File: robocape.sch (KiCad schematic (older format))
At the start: 22 parts

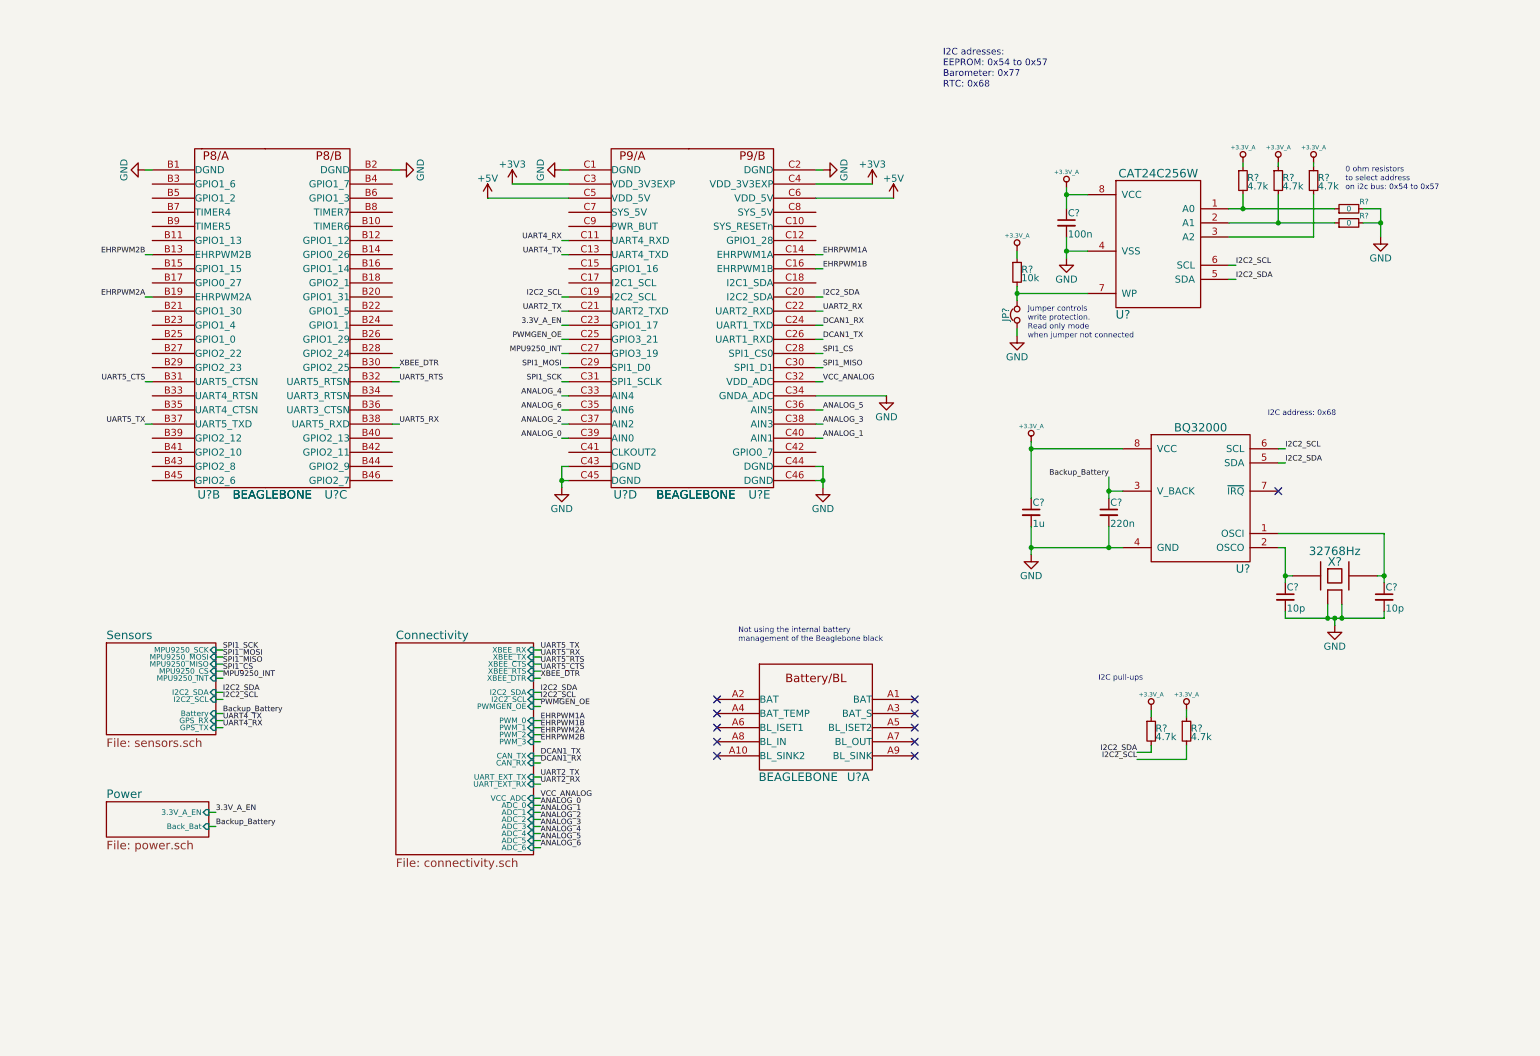
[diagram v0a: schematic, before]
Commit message: Schematics: Minor cleanups
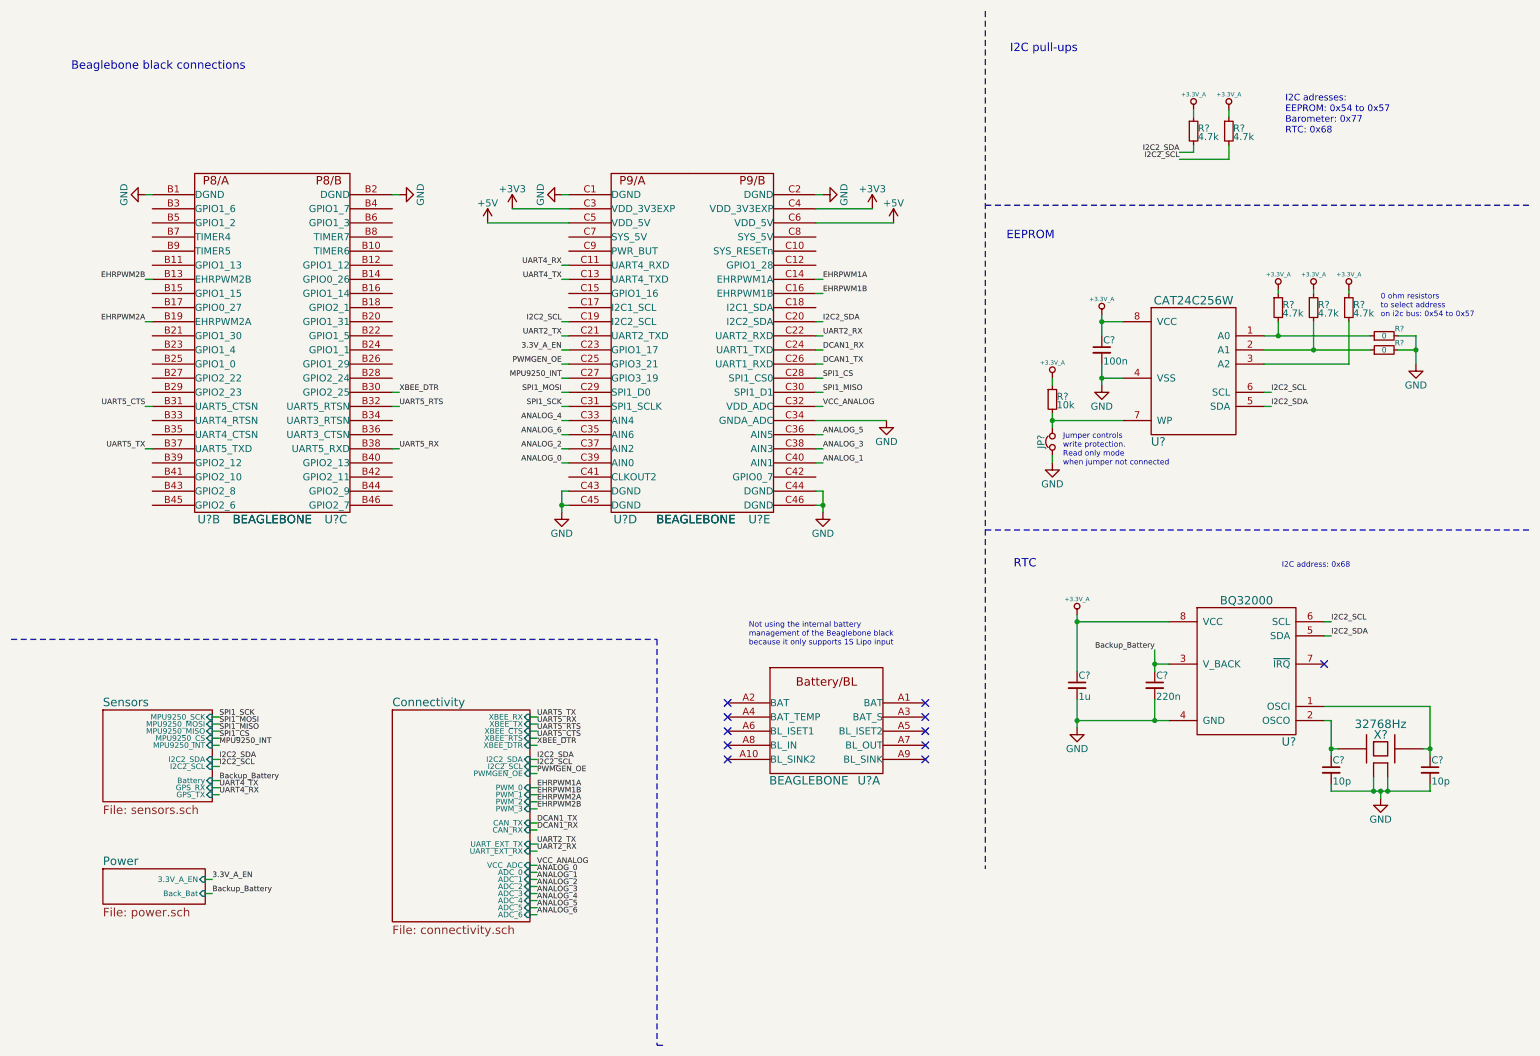
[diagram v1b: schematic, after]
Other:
- note added: "Beaglebone black connections"
- note added: "EEPROM\n"
- note added: "I2C pull-ups"
- note added: "Not using the internal battery\nmanagement of the Beaglebone black\nbecause it only supports 1S Lipo input"
- note added: "RTC"
- note removed: "I2C pull-ups\n"
- note removed: "Not using the internal battery\nmanagement of the Beaglebone black"
- moved on the sheet: C?, JP?, R?, U?, U?A, U?B, U?C, U?D, U?E, X?

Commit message: Schematics: LEDs
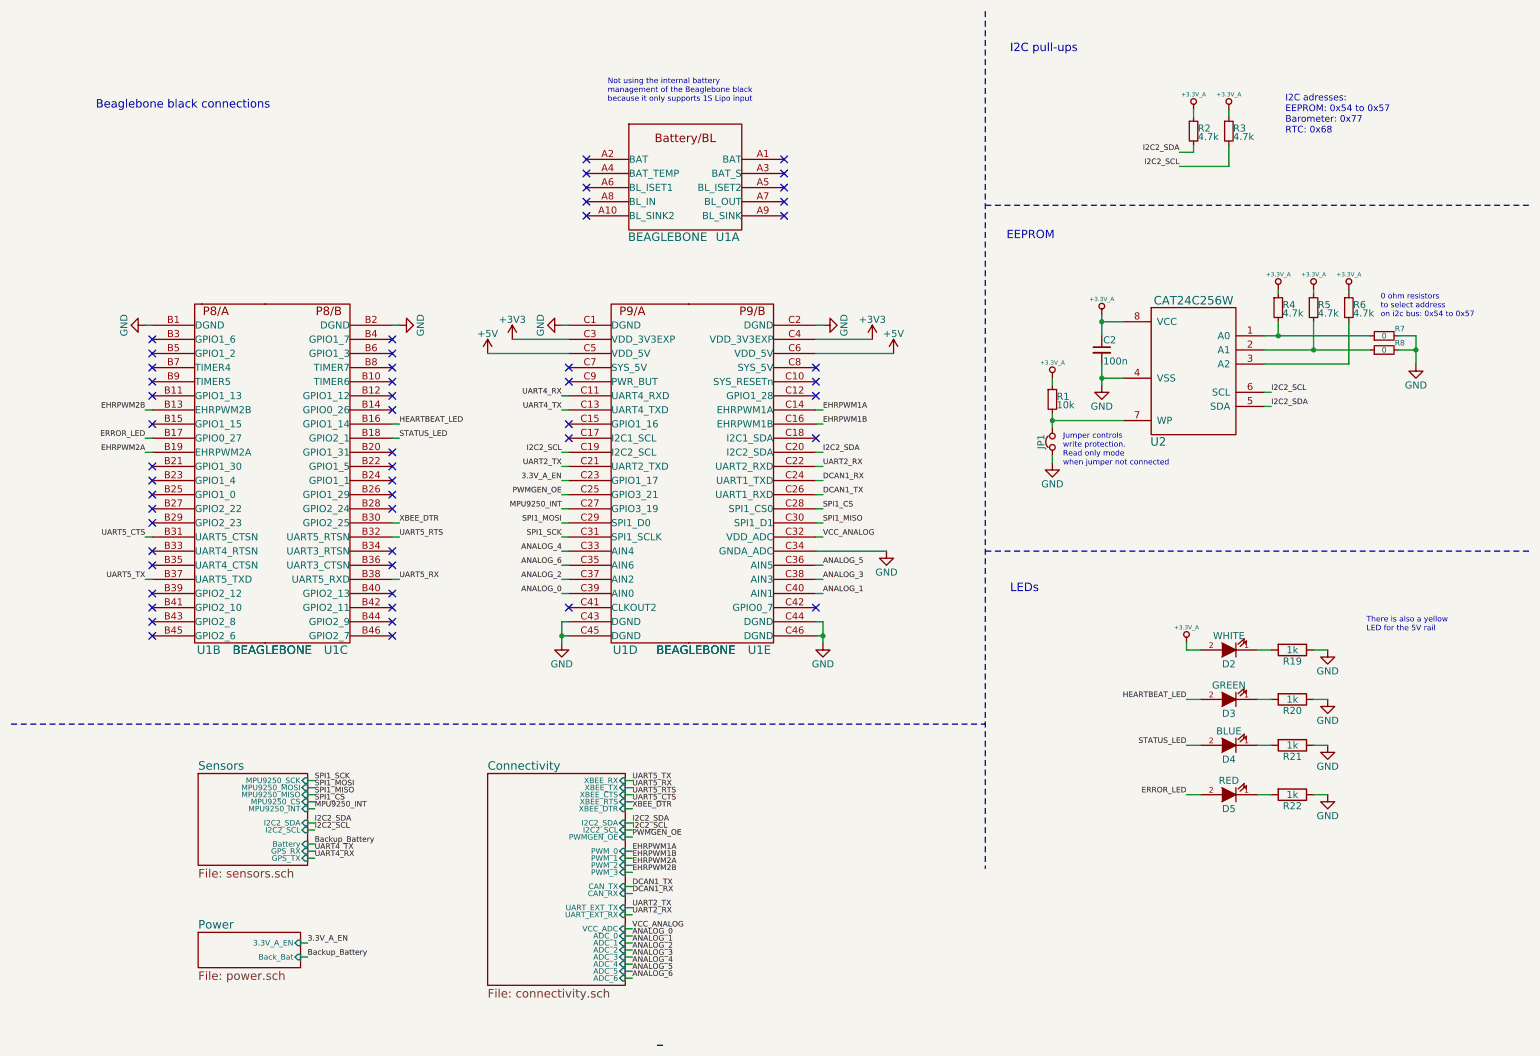
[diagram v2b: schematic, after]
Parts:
- removed C?: 220n, symbol C_Small
- removed C?: 1u, symbol C_Small
- removed C? (x2): 10p, symbol C_Small
- removed U?: BQ32000, symbol BQ32000
- removed X?: 32768Hz, symbol XTAL-SMD-4-PADS
- added D2: WHITE, symbol LED
- added D3: GREEN, symbol LED
- added D4: BLUE, symbol LED
- added D5: RED, symbol LED
- added R19, R20, R21, R22: 1k, symbol R
- gave numbers to parts that had none: 12
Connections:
- net +3.3V_A: now also D2.2 (A)
- net GND: now also R19.1, R20.1, R21.1, R22.1
- net ERROR_LED: now reaches U1.B17 (GPIO0_27)
- net ERROR_LED: now also D5.2 (A)
- net HEARTBEAT_LED: now reaches U1.B16 (GPIO1_14)
- net HEARTBEAT_LED: now also D3.2 (A)
- net STATUS_LED: now reaches U1.B18 (GPIO2_1)
- net STATUS_LED: now also D4.2 (A)
- new net: D2.1 (K), R19.2
- new net: D3.1 (K), R20.2
- new net: D4.1 (K), R21.2
- new net: D5.1 (K), R22.2
- no-connect marks 11 -> 54
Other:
- note added: "LEDs"
- note added: "There is also a yellow \nLED for the 5V rail"
- note removed: "I2C address: 0x68"
- note removed: "RTC"
- moved on the sheet: U1A, U1B, U1C, U1D, U1E

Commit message: Schematics: Additional I2C connector
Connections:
- net I2C1_SCL: now reaches U1.C17 (I2C1_SCL)
- net I2C1_SDA: now reaches U1.C18 (I2C1_SDA)
- no-connect marks 54 -> 52
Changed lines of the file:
@@
 $EndComp
 $Sheet
-S 3850 5875 975  1500
+S 3850 5875 975  1700
 U 55A505CD
 F0 "Connectivity" 60
@@
 F24 "ADC_5" I R 4825 7275 39
 F25 "ADC_6" I R 4825 7325 39
+F26 "I2C1_SDA" I R 4825 7425 39
+F27 "I2C1_SCL" I R 4825 7475 39
 $EndSheet
 $Sheet
@@
 NoConn ~ 6175 3100
 NoConn ~ 6175 3200
-NoConn ~ 6175 3500
 NoConn ~ 6175 4700
 NoConn ~ 4425 4700
-NoConn ~ 4425 3500
 NoConn ~ 4425 3400
 NoConn ~ 4425 3100
@@
 Wire Wire Line
 	1425 3500 1475 3500
+Text Label 4875 7425 0    39   ~ 0
+I2C1_SDA
+Text Label 4875 7475 0    39   ~ 0
+I2C1_SCL
+Wire Wire Line
+	4875 7475 4825 7475
+Wire Wire Line
+	4825 7425 4875 7425
+Text Label 6225 3500 0    39   ~ 0
+I2C1_SDA
+Text Label 4375 3500 2    39   ~ 0
+I2C1_SCL
+Wire Wire Line
+	4375 3500 4425 3500
+Wire Wire Line
+	6225 3500 6175 3500
 $EndSCHEMATC

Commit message: Schematics: Missing I2C1 pull-ups
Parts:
- added R23, R24: 4.7k, symbol R_Small
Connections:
- net +3.3V_A: now also R23.1, R24.1
- net I2C1_SCL: now also R24.2
- net I2C1_SDA: now also R23.2
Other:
- note added: "I2C 2 adresses:\nEEPROM: 0x54 to 0x57\nBarometer: 0x77\nRTC: 0x68"
- note removed: "I2C adresses:\nEEPROM: 0x54 to 0x57\nBarometer: 0x77\nRTC: 0x68"
- moved on the sheet: R2, R3
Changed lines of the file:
@@
 encoding utf-8
 Sheet 1 4
-Title ""
-Date ""
-Rev ""
-Comp ""
-Comment1 ""
+Title "Robotics Cape"
+Date "2015-07-20"
+Rev "C"
+Comp "Automatic Control Laboratory EPFL"
+Comment1 "Designed by: Salah-Eddine Missri"
 Comment2 ""
 Comment3 ""
@@
 $EndComp
 $Comp
-L GND #PWR26
+L GND #PWR27
 U 1 1 55A51ECA
 P 10425 2975
-F 0 "#PWR26" H 10425 2725 50  0001 C CNN
+F 0 "#PWR27" H 10425 2725 50  0001 C CNN
 F 1 "GND" H 10425 2825 50  0000 C CNN
 F 2 "" H 10425 2975 60  0000 C CNN
@@
 Text Label 3225 4100 0    39   ~ 0
 XBEE_DTR
-Text Notes 9500 1350 0    47   ~ 0
-I2C adresses:\nEEPROM: 0x54 to 0x57\nBarometer: 0x77\nRTC: 0x68
-Text Label 8750 1475 2    39   ~ 0
+Text Notes 7875 1475 0    47   ~ 0
+I2C 2 adresses:\nEEPROM: 0x54 to 0x57\nBarometer: 0x77\nRTC: 0x68
+Text Label 9175 1475 2    39   ~ 0
 I2C2_SDA
-Text Label 8750 1575 2    39   ~ 0
+Text Label 9175 1575 2    39   ~ 0
 I2C2_SCL
 $Comp
 L R_Small R2
 U 1 1 55A80D7C
-P 8850 1325
-F 0 "R2" H 8880 1345 50  0000 L CNN
-F 1 "4.7k" H 8880 1285 50  0000 L CNN
-F 2 "" H 8850 1325 60  0000 C CNN
-F 3 "" H 8850 1325 60  0000 C CNN
-	1    8850 1325
+P 9275 1325
+F 0 "R2" H 9305 1345 50  0000 L CNN
+F 1 "4.7k" H 9305 1285 50  0000 L CNN
+F 2 "" H 9275 1325 60  0000 C CNN
+F 3 "" H 9275 1325 60  0000 C CNN
+	1    9275 1325
 	1    0    0    -1
 $EndComp
@@
 L R_Small R3
 U 1 1 55A80E92
-P 9100 1325
-F 0 "R3" H 9130 1345 50  0000 L CNN
-F 1 "4.7k" H 9130 1285 50  0000 L CNN
-F 2 "" H 9100 1325 60  0000 C CNN
-F 3 "" H 9100 1325 60  0000 C CNN
-	1    9100 1325
+P 9525 1325
+F 0 "R3" H 9555 1345 50  0000 L CNN
+F 1 "4.7k" H 9555 1285 50  0000 L CNN
+F 2 "" H 9525 1325 60  0000 C CNN
+F 3 "" H 9525 1325 60  0000 C CNN
+	1    9525 1325
 	1    0    0    -1
 $EndComp
@@
 L +3.3V_A #PWR17
 U 1 1 55A80FFB
-P 8850 1175
-F 0 "#PWR17" H 8850 1135 30  0001 C CNN
-F 1 "+3.3V_A" H 8850 1285 30  0000 C CNN
-F 2 "" H 8850 1175 60  0000 C CNN
-F 3 "" H 8850 1175 60  0000 C CNN
-	1    8850 1175
-	1    0    0    -1
-$EndComp
-$Comp
-L +3.3V_A #PWR18
+P 9275 1175
+F 0 "#PWR17" H 9275 1135 30  0001 C CNN
+F 1 "+3.3V_A" H 9275 1285 30  0000 C CNN
+F 2 "" H 9275 1175 60  0000 C CNN
+F 3 "" H 9275 1175 60  0000 C CNN
+	1    9275 1175
+	1    0    0    -1
+$EndComp
+$Comp
+L +3.3V_A #PWR19
 U 1 1 55A810F5
-P 9100 1175
-F 0 "#PWR18" H 9100 1135 30  0001 C CNN
-F 1 "+3.3V_A" H 9100 1285 30  0000 C CNN
-F 2 "" H 9100 1175 60  0000 C CNN
-F 3 "" H 9100 1175 60  0000 C CNN
-	1    9100 1175
+P 9525 1175
+F 0 "#PWR19" H 9525 1135 30  0001 C CNN
+F 1 "+3.3V_A" H 9525 1285 30  0000 C CNN
+F 2 "" H 9525 1175 60  0000 C CNN
+F 3 "" H 9525 1175 60  0000 C CNN
+	1    9525 1175
 	1    0    0    -1
 $EndComp
@@
 VCC_ANALOG
 Wire Wire Line
-	8200 2625 8200 2775
+	8200 2625 8200 2675
+Wire Wire Line
+	8200 2675 8200 2775
 Wire Wire Line
 	8200 2675 8350 2675
 Connection ~ 8200 2675
 Wire Wire Line
-	8200 2975 8200 3125
+	8200 2975 8200 3075
+Wire Wire Line
+	8200 3075 8200 3125
 Wire Wire Line
 	8200 3075 8350 3075
 Connection ~ 8200 3075
 Wire Wire Line
-	7850 3325 7850 3425
+	7850 3325 7850 3375
+Wire Wire Line
+	7850 3375 7850 3425
 Wire Wire Line
 	7850 3375 8350 3375
@@
 	9450 2675 9450 2775
 Wire Wire Line
-	9350 2775 10100 2775
-Wire Wire Line
-	9350 2875 10100 2875
+	9350 2775 9450 2775
+Wire Wire Line
+	9450 2775 10100 2775
+Wire Wire Line
+	9350 2875 9700 2875
+Wire Wire Line
+	9700 2875 10100 2875
 Wire Wire Line
 	9700 2875 9700 2675
@@
 Connection ~ 9450 2775
 Wire Wire Line
-	10425 2775 10425 2975
+	10425 2775 10425 2875
+Wire Wire Line
+	10425 2875 10425 2975
 Wire Wire Line
 	10425 2875 10300 2875
@@
 	4375 4000 4425 4000
 Wire Wire Line
-	8750 1475 8850 1475
-Wire Wire Line
-	8850 1475 8850 1425
-Wire Wire Line
-	8750 1575 9100 1575
-Wire Wire Line
-	9100 1575 9100 1425
-Wire Wire Line
-	8850 1175 8850 1225
-Wire Wire Line
-	9100 1175 9100 1225
+	9175 1475 9275 1475
+Wire Wire Line
+	9275 1475 9275 1425
+Wire Wire Line
+	9175 1575 9525 1575
+Wire Wire Line
+	9525 1575 9525 1425
+Wire Wire Line
+	9275 1175 9275 1225
+Wire Wire Line
+	9525 1175 9525 1225
 Wire Wire Line
 	6225 3400 6175 3400
@@
 	4375 2700 4425 2700
 Wire Wire Line
-	4375 4800 4375 4950
+	4375 4800 4375 4900
+Wire Wire Line
+	4375 4900 4375 4950
 Wire Wire Line
 	4375 4900 4425 4900
@@
 Connection ~ 4375 4900
 Wire Wire Line
-	6225 4800 6225 4950
+	6225 4800 6225 4900
+Wire Wire Line
+	6225 4900 6225 4950
 Wire Wire Line
 	6225 4900 6175 4900
@@
 $EndComp
 $Comp
-L +3.3V_A #PWR19
+L +3.3V_A #PWR18
 U 1 1 55ADFA9B
 P 9450 2450
-F 0 "#PWR19" H 9450 2410 30  0001 C CNN
+F 0 "#PWR18" H 9450 2410 30  0001 C CNN
 F 1 "+3.3V_A" H 9450 2560 30  0000 C CNN
 F 2 "" H 9450 2450 60  0000 C CNN
@@
 Wire Wire Line
 	6225 3500 6175 3500
+Text Label 10250 1475 2    39   ~ 0
+I2C1_SDA
+Text Label 10250 1575 2    39   ~ 0
+I2C1_SCL
+$Comp
+L R_Small R23
+U 1 1 55B29E4E
+P 10350 1325
+F 0 "R23" H 10380 1345 50  0000 L CNN
+F 1 "4.7k" H 10380 1285 50  0000 L CNN
+F 2 "" H 10350 1325 60  0000 C CNN
+F 3 "" H 10350 1325 60  0000 C CNN
+	1    10350 1325
+	1    0    0    -1
+$EndComp
+$Comp
+L R_Small R24
+U 1 1 55B29E54
+P 10600 1325
+F 0 "R24" H 10630 1345 50  0000 L CNN
+F 1 "4.7k" H 10630 1285 50  0000 L CNN
+F 2 "" H 10600 1325 60  0000 C CNN
+F 3 "" H 10600 1325 60  0000 C CNN
+	1    10600 1325
+	1    0    0    -1
+$EndComp
+$Comp
+L +3.3V_A #PWR26
+U 1 1 55B29E5A
+P 10350 1175
+F 0 "#PWR26" H 10350 1135 30  0001 C CNN
+F 1 "+3.3V_A" H 10350 1285 30  0000 C CNN
+F 2 "" H 10350 1175 60  0000 C CNN
+F 3 "" H 10350 1175 60  0000 C CNN
+	1    10350 1175
+	1    0    0    -1
+$EndComp
+$Comp
+L +3.3V_A #PWR28
+U 1 1 55B29E60
+P 10600 1175
+F 0 "#PWR28" H 10600 1135 30  0001 C CNN
+F 1 "+3.3V_A" H 10600 1285 30  0000 C CNN
+F 2 "" H 10600 1175 60  0000 C CNN
+F 3 "" H 10600 1175 60  0000 C CNN
+	1    10600 1175
+	1    0    0    -1
+$EndComp
+Wire Wire Line
+	10250 1475 10350 1475
+Wire Wire Line
+	10350 1475 10350 1425
+Wire Wire Line
+	10250 1575 10600 1575
+Wire Wire Line
+	10600 1575 10600 1425
+Wire Wire Line
+	10350 1175 10350 1225
+Wire Wire Line
+	10600 1175 10600 1225
 $EndSCHEMATC

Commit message: Schematics: SPI connector
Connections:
- net SPI1_CS1: now reaches U1.C42 (GPIO0_7)
- net SPI1_CS renamed SPI1_CS0
- no-connect marks 52 -> 51
